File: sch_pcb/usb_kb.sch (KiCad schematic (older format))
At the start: 6 parts, among them P1 USB_C_Plug, U1 STM32F103C6Tx, U2 USBLC6-2SC6

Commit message: Андрей изменил схему, добавил стабилизатор
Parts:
- added C1, C3: 1uF, Capacitor_SMD:C_0805_2012Metric_Pad1.15x1.40mm_HandSolder, symbol Device:C
- added C2, C4: 0.1uF, Capacitor_SMD:C_0805_2012Metric_Pad1.15x1.40mm_HandSolder, symbol Device:C
- added D1: D_Schottky, Diode_SMD:D_SMA, symbol Device:D_Schottky
- added U3: AMS1117-3.3, Package_TO_SOT_SMD:SOT-223-3_TabPin2, symbol Regulator_Linear:AMS1117-3.3
- P1: symbol Connector:USB_C_Plug -> usb_kb-rescue:USB_C_Plug-Connector
- U2: value USBLC6-2SC6 -> AMS1117-3.3; footprint Package_TO_SOT_SMD:SOT-23-6 -> (none); symbol Power_Protection:USBLC6-2SC6 -> usb_kb-rescue:USBLC6-2SC6-Power_Protection
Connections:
- net labels added: +3.3V
- wire segments 26 -> 47
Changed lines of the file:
@@
 $EndDescr
 $Comp
-L Connector:USB_C_Plug P1
+L usb_kb-rescue:USB_C_Plug-Connector P1
 U 1 1 6152BA8E
 P 2100 3100
@@
 $EndComp
 $Comp
-L Power_Protection:USBLC6-2SC6 U2
+L usb_kb-rescue:USBLC6-2SC6-Power_Protection U2
 U 1 1 6153205F
 P 4550 2700
 F 0 "U2" H 4550 3381 50  0000 C CNN
-F 1 "USBLC6-2SC6" H 4550 3290 50  0000 C CNN
-F 2 "Package_TO_SOT_SMD:SOT-23-6" H 3800 3100 50  0001 C CNN
+F 1 "AMS1117-3.3" H 4550 3290 50  0000 C CNN
+F 2 "" H 3800 3100 50  0001 C CNN
 F 3 "http://www2.st.com/resource/en/datasheet/CD00050750.pdf" H 4750 3050 50  0001 C CNN
 	1    4550 2700
@@
 L power:+5V #PWR0101
 U 1 1 61544FD7
-P 2700 1800
-F 0 "#PWR0101" H 2700 1650 50  0001 C CNN
-F 1 "+5V" H 2715 1973 50  0000 C CNN
-F 2 "" H 2700 1800 50  0001 C CNN
-F 3 "" H 2700 1800 50  0001 C CNN
-	1    2700 1800
+P 2900 1300
+F 0 "#PWR0101" H 2900 1150 50  0001 C CNN
+F 1 "+5V" H 2915 1473 50  0000 C CNN
+F 2 "" H 2900 1300 50  0001 C CNN
+F 3 "" H 2900 1300 50  0001 C CNN
+	1    2900 1300
 	1    0    0    -1
 $EndComp
@@
 Wire Wire Line
 	5100 2700 5100 2900
-Wire Wire Line
-	2700 1800 2700 2100
 $Comp
 L power:GNDD #PWR0103
@@
 Wire Wire Line
 	9350 4350 9650 4350
+$Comp
+L Device:C C2
+U 1 1 61570A54
+P 4100 4700
+F 0 "C2" H 4215 4746 50  0000 L CNN
+F 1 "0.1uF" H 4215 4655 50  0000 L CNN
+F 2 "Capacitor_SMD:C_0805_2012Metric_Pad1.15x1.40mm_HandSolder" H 4138 4550 50  0001 C CNN
+F 3 "~" H 4100 4700 50  0001 C CNN
+	1    4100 4700
+	1    0    0    -1
+$EndComp
+$Comp
+L power:+5V #PWR0107
+U 1 1 61580B5F
+P 3750 4300
+F 0 "#PWR0107" H 3750 4150 50  0001 C CNN
+F 1 "+5V" H 3765 4473 50  0000 C CNN
+F 2 "" H 3750 4300 50  0001 C CNN
+F 3 "" H 3750 4300 50  0001 C CNN
+	1    3750 4300
+	1    0    0    -1
+$EndComp
+Wire Wire Line
+	4100 4850 4100 4950
+Wire Wire Line
+	4100 4950 3750 4950
+Wire Wire Line
+	3750 4950 3750 4850
+$Comp
+L power:GNDD #PWR01
+U 1 1 6155592B
+P 3750 5100
+F 0 "#PWR01" H 3750 4850 50  0001 C CNN
+F 1 "GNDD" H 3754 4945 50  0000 C CNN
+F 2 "" H 3750 5100 50  0001 C CNN
+F 3 "" H 3750 5100 50  0001 C CNN
+	1    3750 5100
+	1    0    0    -1
+$EndComp
+Wire Wire Line
+	3750 4950 3750 5100
+Connection ~ 3750 4950
+$Comp
+L power:+3.3V #PWR03
+U 1 1 615606CF
+P 5550 4300
+F 0 "#PWR03" H 5550 4150 50  0001 C CNN
+F 1 "+3.3V" H 5565 4473 50  0000 C CNN
+F 2 "" H 5550 4300 50  0001 C CNN
+F 3 "" H 5550 4300 50  0001 C CNN
+	1    5550 4300
+	1    0    0    -1
+$EndComp
+Wire Wire Line
+	4950 4450 5200 4450
+Wire Wire Line
+	4350 4450 4100 4450
+Wire Wire Line
+	3750 4450 3750 4550
+Wire Wire Line
+	3750 4300 3750 4450
+Connection ~ 3750 4450
+Wire Wire Line
+	4100 4550 4100 4450
+Connection ~ 4100 4450
+Wire Wire Line
+	4100 4450 3750 4450
+Wire Wire Line
+	5200 4550 5200 4450
+Connection ~ 5200 4450
+Wire Wire Line
+	5200 4450 5550 4450
+Wire Wire Line
+	5550 4550 5550 4450
+Wire Wire Line
+	5200 4850 5200 4950
+Wire Wire Line
+	5200 4950 5550 4950
+Wire Wire Line
+	5550 4950 5550 4850
+$Comp
+L power:GNDD #PWR02
+U 1 1 615895AD
+P 4650 5100
+F 0 "#PWR02" H 4650 4850 50  0001 C CNN
+F 1 "GNDD" H 4654 4945 50  0000 C CNN
+F 2 "" H 4650 5100 50  0001 C CNN
+F 3 "" H 4650 5100 50  0001 C CNN
+	1    4650 5100
+	1    0    0    -1
+$EndComp
+$Comp
+L power:GNDD #PWR04
+U 1 1 6158D0F6
+P 5550 5100
+F 0 "#PWR04" H 5550 4850 50  0001 C CNN
+F 1 "GNDD" H 5554 4945 50  0000 C CNN
+F 2 "" H 5550 5100 50  0001 C CNN
+F 3 "" H 5550 5100 50  0001 C CNN
+	1    5550 5100
+	1    0    0    -1
+$EndComp
+Wire Wire Line
+	4650 4750 4650 5100
+Wire Wire Line
+	5550 4950 5550 5100
+Connection ~ 5550 4950
+$Comp
+L Device:C C1
+U 1 1 6159B622
+P 3750 4700
+F 0 "C1" H 3865 4746 50  0000 L CNN
+F 1 "1uF" H 3865 4655 50  0000 L CNN
+F 2 "Capacitor_SMD:C_0805_2012Metric_Pad1.15x1.40mm_HandSolder" H 3788 4550 50  0001 C CNN
+F 3 "~" H 3750 4700 50  0001 C CNN
+	1    3750 4700
+	1    0    0    -1
+$EndComp
+$Comp
+L Device:C C4
+U 1 1 615A45E7
+P 5550 4700
+F 0 "C4" H 5665 4746 50  0000 L CNN
+F 1 "0.1uF" H 5665 4655 50  0000 L CNN
+F 2 "Capacitor_SMD:C_0805_2012Metric_Pad1.15x1.40mm_HandSolder" H 5588 4550 50  0001 C CNN
+F 3 "~" H 5550 4700 50  0001 C CNN
+	1    5550 4700
+	1    0    0    -1
+$EndComp
+$Comp
+L Device:C C3
+U 1 1 615A45ED
+P 5200 4700
+F 0 "C3" H 5315 4746 50  0000 L CNN
+F 1 "1uF" H 5315 4655 50  0000 L CNN
+F 2 "Capacitor_SMD:C_0805_2012Metric_Pad1.15x1.40mm_HandSolder" H 5238 4550 50  0001 C CNN
+F 3 "~" H 5200 4700 50  0001 C CNN
+	1    5200 4700
+	1    0    0    -1
+$EndComp
+Wire Wire Line
+	5550 4300 5550 4450
+Connection ~ 5550 4450
+$Comp
+L Regulator_Linear:AMS1117-3.3 U3
+U 1 1 615B256A
+P 4650 4450
+F 0 "U3" H 4650 4692 50  0000 C CNN
+F 1 "AMS1117-3.3" H 4650 4601 50  0000 C CNN
+F 2 "Package_TO_SOT_SMD:SOT-223-3_TabPin2" H 4650 4650 50  0001 C CNN
+F 3 "http://www.advanced-monolithic.com/pdf/ds1117.pdf" H 4750 4200 50  0001 C CNN
+	1    4650 4450
+	1    0    0    -1
+$EndComp
+$Comp
+L Device:D_Schottky D1
+U 1 1 615BE243
+P 2900 1650
+F 0 "D1" V 2854 1729 50  0000 L CNN
+F 1 "D_Schottky" V 2945 1729 50  0000 L CNN
+F 2 "Diode_SMD:D_SMA" H 2900 1650 50  0001 C CNN
+F 3 "~" H 2900 1650 50  0001 C CNN
+	1    2900 1650
+	0    1    1    0
+$EndComp
+Wire Wire Line
+	2700 2100 2900 2100
+Wire Wire Line
+	2900 2100 2900 1800
+Wire Wire Line
+	2900 1500 2900 1300
 $EndSCHEMATC

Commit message: Андрей добавил питание, Никита доделал
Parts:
- added C10, C9: 20pF, Capacitor_SMD:C_0805_2012Metric_Pad1.15x1.40mm_HandSolder, symbol Device:C
- added C11, C5, C6, C7, C8: 100nF, Capacitor_SMD:C_0805_2012Metric_Pad1.15x1.40mm_HandSolder, symbol Device:C
- added C12, C13: 47nF, Capacitor_SMD:C_0805_2012Metric_Pad1.15x1.40mm_HandSolder, symbol Device:C
- added JP2: Jumper, Jumper:SolderJumper-2_P1.3mm_Open_TrianglePad1.0x1.5mm, symbol Device:Jumper
- added R3, R6: 10k, Resistor_SMD:R_0603_1608Metric_Pad1.05x0.95mm_HandSolder, symbol Device:R
- added R4: 1M, Resistor_SMD:R_0603_1608Metric_Pad1.05x0.95mm_HandSolder, symbol Device:R
- added R5: 1.5k, Resistor_SMD:R_0603_1608Metric_Pad1.05x0.95mm_HandSolder, symbol Device:R
- added X1: 8MHz, Crystal:Crystal_HC49-4H_Vertical, symbol Device:Crystal
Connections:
- net +3V3: now also U1.24 (VDD), U1.36 (VDD), U1.48 (VDD), U1.9 (VDDA), U2.5 (VBUS), C5.1, C6.1, C7.1, C8.1, JP2.2, R3.1, R5.1
- net GNDD: now also U1.23 (VSS), U1.35 (VSS), U1.47 (VSS), U1.8 (VSSA), C10.2, C11.2, C12.2, C13.2, C5.2, C6.2, C7.2, C8.2, C9.2, R6.2
- net USB_D+: now also U2.1 (IO1), U2.6 (IO1), C13.1, R5.2
- net USB_D-: now also U2.3 (IO2), U2.4 (IO2), C12.1
- net at P1.A6 (D+), R2.2: no longer U2.1 (IO1), U2.6 (IO1)
- net at P1.A7 (D-), R1.2: no longer U2.3 (IO2), U2.4 (IO2)
- net at U1.1 (VBAT): now also JP2.1
- net BOOT0: now reaches U1.44 (BOOT0)
- net BOOT0: now also R6.1
- net at U1.5 (PD0): now also C9.1, R4.1, X1.1
- net at U1.6 (PD1): now also C10.1, R4.2, X1.2
- net RST: now reaches U1.7 (NRST)
- net RST: now also C11.1, R3.2
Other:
- moved on the sheet: C1, C2, C3, C4, R1, R2, U1, U3

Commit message: Добавлена кнопа и мелкие правки
Добавлена кнопа и мелкие правки

Co-Authored-By: Andrey2312 <91528901+Andrey2312@users.noreply.github.com>
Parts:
- removed U2: AMS1117-3.3, symbol usb_kb-rescue:USBLC6-2SC6-Power_Protection
- added C14: 0.1uF, Capacitor_SMD:C_0805_2012Metric_Pad1.15x1.40mm_HandSolder, symbol Device:C
- added D2, D3, D4: LED_ALT, Diode_SMD:D_0805_2012Metric_Pad1.15x1.40mm_HandSolder, symbol Device:LED_ALT
- added J1: Conn_01x04_Female, Connector_PinHeader_2.54mm:PinHeader_1x04_P2.54mm_Vertical, symbol Connector:Conn_01x04_Female
- added R10: 10k, Resistor_SMD:R_0603_1608Metric_Pad1.05x0.95mm_HandSolder, symbol Device:R
- added R11, R7, R8: 510, Resistor_SMD:R_0603_1608Metric_Pad1.05x0.95mm_HandSolder, symbol Device:R
- added R9: 100, Resistor_SMD:R_0603_1608Metric_Pad1.05x0.95mm_HandSolder, symbol Device:R
- added SW1: SW_Push, Button_Switch_Keyboard:SW_Cherry_MX_1.00u_PCB, symbol Switch:SW_Push
- added U2: USBLC6-2SC6, Package_TO_SOT_SMD:SOT-23-6, symbol Power_Protection:USBLC6-2SC6
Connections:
- net labels added: Button1, Button2
- wire segments 114 -> 140
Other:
- note added: "НЕ МЕНЯЙ ЭЛЕМЕНТЫ НА 0603 В КОТОРЫХ НЕ УВЕРЕН!!!"
- note added: "Разъём программирования"
- note added: "Сюда повторить кнопку, которая сверху"
- moved on the sheet: C1, C2, C3, C4, R6, U3

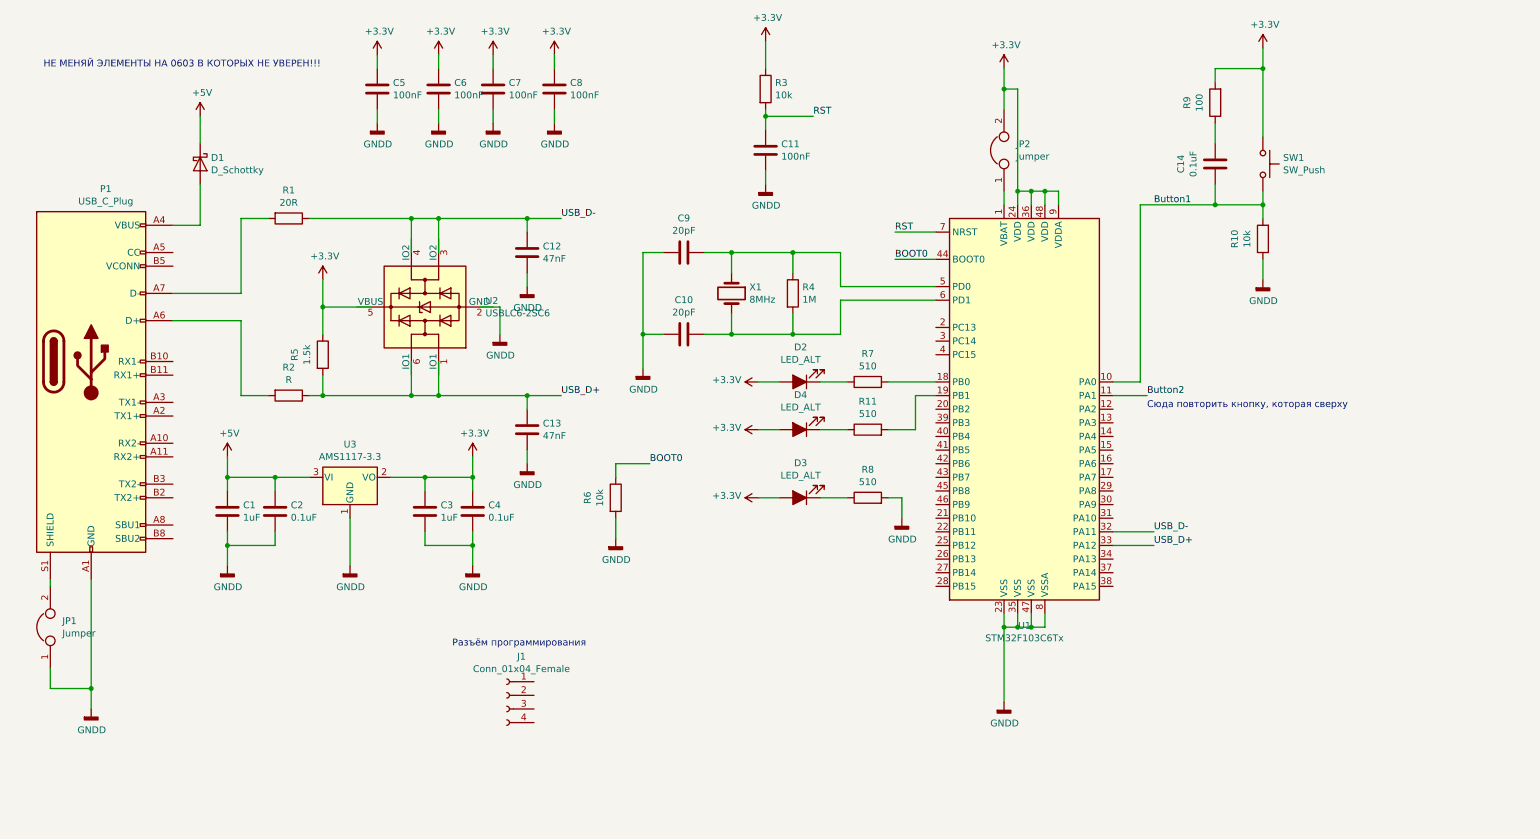
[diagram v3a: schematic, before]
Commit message: ошибка R11. Конечный вариант
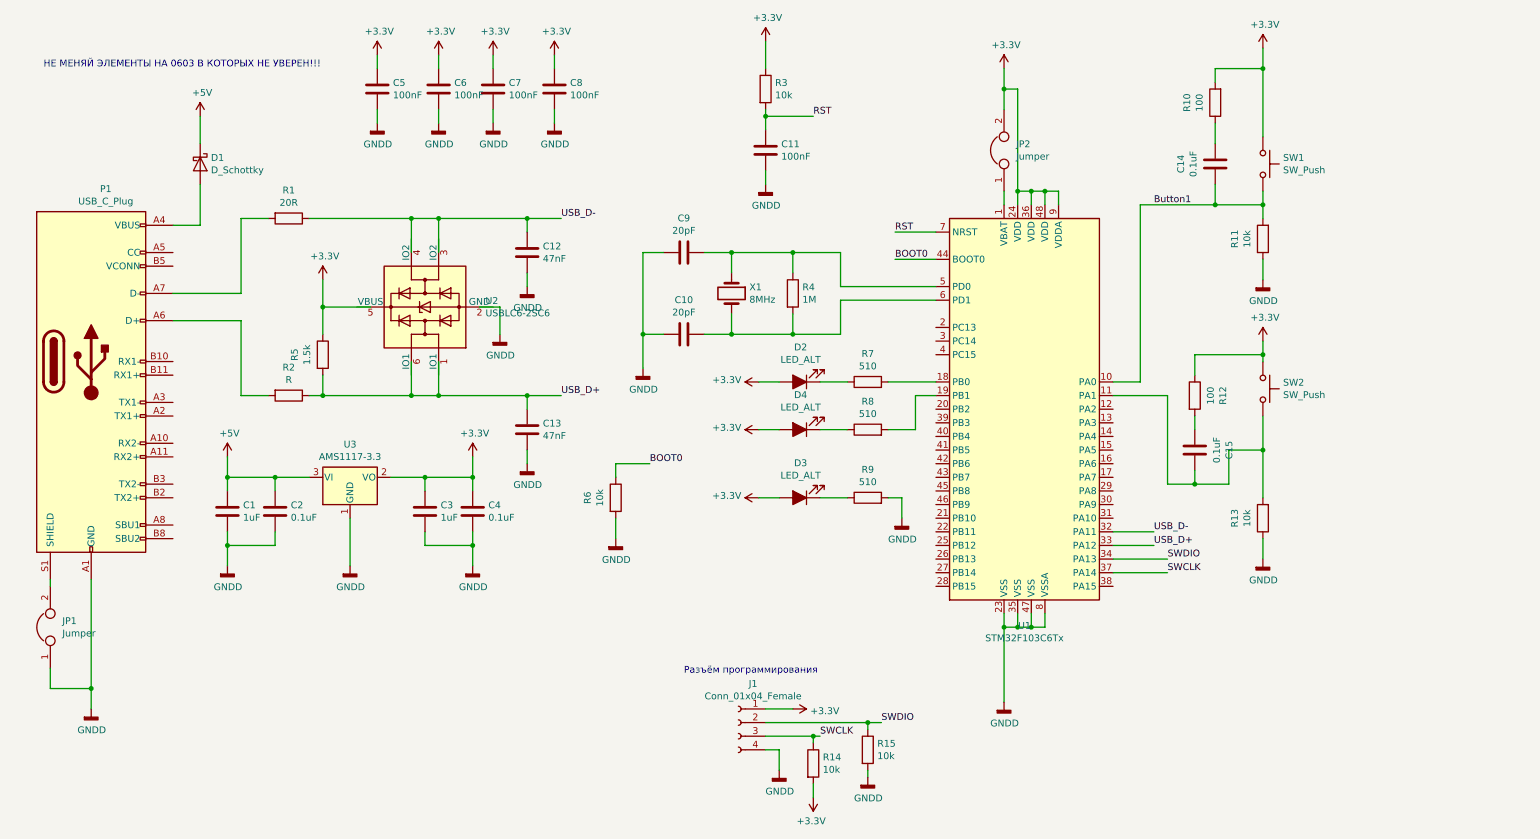
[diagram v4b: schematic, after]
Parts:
- added C15: 0.1uF, Capacitor_SMD:C_0805_2012Metric_Pad1.15x1.40mm_HandSolder, symbol Device:C
- added R12: 100, Resistor_SMD:R_0603_1608Metric_Pad1.05x0.95mm_HandSolder, symbol Device:R
- added R13, R14, R15: 10k, Resistor_SMD:R_0603_1608Metric_Pad1.05x0.95mm_HandSolder, symbol Device:R
- added SW2: SW_Push, Button_Switch_Keyboard:SW_Cherry_MX_1.00u_PCB, symbol Switch:SW_Push
- renumbered R9 to R10, R10 to R11, R11 to R8, R8 to R9
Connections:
- net labels added: SWCLK, SWDIO
- net labels removed: Button2
- wire segments 140 -> 167
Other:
- note removed: "Сюда повторить кнопку, которая сверху"
- moved on the sheet: J1
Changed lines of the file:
@@
 $EndComp
 $Comp
-L Device:R R8
+L Device:R R9
 U 1 1 615BC881
 P 7800 4100
-F 0 "R8" V 8007 4100 50  0000 C CNN
+F 0 "R9" V 8007 4100 50  0000 C CNN
 F 1 "510" V 7916 4100 50  0000 C CNN
 F 2 "Resistor_SMD:R_0603_1608Metric_Pad1.05x0.95mm_HandSolder" V 7730 4100 50  0001 C CNN
@@
 $EndComp
 $Comp
-L Device:R R9
+L Device:R R10
 U 1 1 61563424
 P 10350 1200
-F 0 "R9" V 10557 1200 50  0000 C CNN
+F 0 "R10" V 10557 1200 50  0000 C CNN
 F 1 "100" V 10466 1200 50  0000 C CNN
 F 2 "Resistor_SMD:R_0603_1608Metric_Pad1.05x0.95mm_HandSolder" V 10280 1200 50  0001 C CNN
@@
 $EndComp
 $Comp
-L Device:R R10
+L Device:R R11
 U 1 1 61567374
 P 10700 2200
-F 0 "R10" V 10907 2200 50  0000 C CNN
+F 0 "R11" V 10907 2200 50  0000 C CNN
 F 1 "10k" V 10816 2200 50  0000 C CNN
 F 2 "Resistor_SMD:R_0603_1608Metric_Pad1.05x0.95mm_HandSolder" V 10630 2200 50  0001 C CNN
@@
 Text Label 9900 1950 0    50   ~ 0
 Button1
-Text Label 9850 3350 0    50   ~ 0
-Button2
-Wire Wire Line
-	9850 3350 9600 3350
 $Comp
 L Device:LED_ALT D4
@@
 $EndComp
 $Comp
-L Device:R R11
+L Device:R R8
 U 1 1 615B3C09
 P 7800 3600
-F 0 "R11" V 8007 3600 50  0000 C CNN
+F 0 "R8" V 8007 3600 50  0000 C CNN
 F 1 "510" V 7916 3600 50  0000 C CNN
 F 2 "Resistor_SMD:R_0603_1608Metric_Pad1.05x0.95mm_HandSolder" V 7730 3600 50  0001 C CNN
@@
 Wire Wire Line
 	7950 3250 8300 3250
-Text Notes 9850 3450 0    50   ~ 0
-Сюда повторить кнопку, которая сверху
-$Comp
-L Connector:Conn_01x04_Female J1
-U 1 1 615DD6C5
-P 5150 5550
-F 0 "J1" H 5042 5835 50  0000 C CNN
-F 1 "Conn_01x04_Female" H 5042 5744 50  0000 C CNN
-F 2 "Connector_PinHeader_2.54mm:PinHeader_1x04_P2.54mm_Vertical" H 5150 5550 50  0001 C CNN
-F 3 "~" H 5150 5550 50  0001 C CNN
-	1    5150 5550
-	-1   0    0    -1
-$EndComp
-Text Notes 4750 5200 0    50   ~ 0
-Разъём программирования
 Text Notes 1750 950  0    50   ~ 0
 НЕ МЕНЯЙ ЭЛЕМЕНТЫ НА 0603 В КОТОРЫХ НЕ УВЕРЕН!!!
@@
 Wire Wire Line
 	3800 2700 4150 2700
+$Comp
+L Switch:SW_Push SW2
+U 1 1 615AD94E
+P 10700 3300
+F 0 "SW2" V 10654 3448 50  0000 L CNN
+F 1 "SW_Push" V 10745 3448 50  0000 L CNN
+F 2 "Button_Switch_Keyboard:SW_Cherry_MX_1.00u_PCB" H 10700 3500 50  0001 C CNN
+F 3 "~" H 10700 3500 50  0001 C CNN
+	1    10700 3300
+	0    1    1    0
+$EndComp
+$Comp
+L Device:R R13
+U 1 1 615C8D27
+P 10700 4250
+F 0 "R13" V 10907 4250 50  0000 C CNN
+F 1 "10k" V 10816 4250 50  0000 C CNN
+F 2 "Resistor_SMD:R_0603_1608Metric_Pad1.05x0.95mm_HandSolder" V 10630 4250 50  0001 C CNN
+F 3 "~" H 10700 4250 50  0001 C CNN
+	1    10700 4250
+	-1   0    0    1
+$EndComp
+$Comp
+L power:GNDD #PWR031
+U 1 1 615C8D2D
+P 10700 4550
+F 0 "#PWR031" H 10700 4300 50  0001 C CNN
+F 1 "GNDD" H 10704 4395 50  0000 C CNN
+F 2 "" H 10700 4550 50  0001 C CNN
+F 3 "" H 10700 4550 50  0001 C CNN
+	1    10700 4550
+	1    0    0    -1
+$EndComp
+Wire Wire Line
+	10700 4550 10700 4400
+$Comp
+L power:+3.3V #PWR030
+U 1 1 61704C01
+P 10700 2950
+F 0 "#PWR030" H 10700 2800 50  0001 C CNN
+F 1 "+3.3V" H 10715 3123 50  0000 C CNN
+F 2 "" H 10700 2950 50  0001 C CNN
+F 3 "" H 10700 2950 50  0001 C CNN
+	1    10700 2950
+	1    0    0    -1
+$EndComp
+Wire Wire Line
+	10700 3100 10700 3050
+$Comp
+L Device:R R12
+U 1 1 61584F00
+P 10200 3350
+F 0 "R12" V 10407 3350 50  0000 C CNN
+F 1 "100" V 10316 3350 50  0000 C CNN
+F 2 "Resistor_SMD:R_0603_1608Metric_Pad1.05x0.95mm_HandSolder" V 10130 3350 50  0001 C CNN
+F 3 "~" H 10200 3350 50  0001 C CNN
+	1    10200 3350
+	1    0    0    -1
+$EndComp
+$Comp
+L Device:C C15
+U 1 1 61594438
+P 10200 3750
+F 0 "C15" V 9948 3750 50  0000 C CNN
+F 1 "0.1uF" V 10039 3750 50  0000 C CNN
+F 2 "Capacitor_SMD:C_0805_2012Metric_Pad1.15x1.40mm_HandSolder" H 10238 3600 50  0001 C CNN
+F 3 "~" H 10200 3750 50  0001 C CNN
+	1    10200 3750
+	-1   0    0    1
+$EndComp
+Wire Wire Line
+	10000 3350 9600 3350
+Wire Wire Line
+	10200 3200 10200 3050
+Wire Wire Line
+	10200 3050 10700 3050
+Connection ~ 10700 3050
+Wire Wire Line
+	10700 3050 10700 2950
+Wire Wire Line
+	10700 3500 10700 3750
+Wire Wire Line
+	10450 4000 10450 3750
+Wire Wire Line
+	10450 3750 10700 3750
+Wire Wire Line
+	10000 4000 10200 4000
+Wire Wire Line
+	10000 4000 10000 3350
+Connection ~ 10700 3750
+Wire Wire Line
+	10700 3750 10700 4100
+Wire Wire Line
+	10200 3900 10200 4000
+Connection ~ 10200 4000
+Wire Wire Line
+	10200 4000 10450 4000
+Wire Wire Line
+	10200 3500 10200 3600
+Wire Wire Line
+	7050 5950 7150 5950
+Wire Wire Line
+	7150 5950 7150 6100
+$Comp
+L power:GNDD #PWR028
+U 1 1 615C7D1A
+P 7150 6100
+F 0 "#PWR028" H 7150 5850 50  0001 C CNN
+F 1 "GNDD" H 7154 5945 50  0000 C CNN
+F 2 "" H 7150 6100 50  0001 C CNN
+F 3 "" H 7150 6100 50  0001 C CNN
+	1    7150 6100
+	1    0    0    -1
+$EndComp
+Wire Wire Line
+	7050 5650 7250 5650
+$Comp
+L power:+3.3V #PWR029
+U 1 1 615B9365
+P 7250 5650
+F 0 "#PWR029" H 7250 5500 50  0001 C CNN
+F 1 "+3.3V" V 7265 5778 50  0000 L CNN
+F 2 "" H 7250 5650 50  0001 C CNN
+F 3 "" H 7250 5650 50  0001 C CNN
+	1    7250 5650
+	0    1    1    0
+$EndComp
+Text Notes 6450 5400 0    50   ~ 0
+Разъём программирования
+$Comp
+L Connector:Conn_01x04_Female J1
+U 1 1 615DD6C5
+P 6850 5750
+F 0 "J1" H 6742 6035 50  0000 C CNN
+F 1 "Conn_01x04_Female" H 6742 5944 50  0000 C CNN
+F 2 "Connector_PinHeader_2.54mm:PinHeader_1x04_P2.54mm_Vertical" H 6850 5750 50  0001 C CNN
+F 3 "~" H 6850 5750 50  0001 C CNN
+	1    6850 5750
+	-1   0    0    -1
+$EndComp
+Text Label 7900 5750 0    50   ~ 0
+SWDIO
+Wire Wire Line
+	7050 5750 7800 5750
+Text Label 10000 4550 0    50   ~ 0
+SWDIO
+Wire Wire Line
+	9600 4550 10000 4550
+Text Label 7450 5850 0    50   ~ 0
+SWCLK
+Wire Wire Line
+	7050 5850 7400 5850
+Text Label 10000 4650 0    50   ~ 0
+SWCLK
+Wire Wire Line
+	9600 4650 10000 4650
+$Comp
+L Device:R R15
+U 1 1 616A4701
+P 7800 5950
+F 0 "R15" H 7870 5996 50  0000 L CNN
+F 1 "10k" H 7870 5905 50  0000 L CNN
+F 2 "Resistor_SMD:R_0603_1608Metric_Pad1.05x0.95mm_HandSolder" V 7730 5950 50  0001 C CNN
+F 3 "~" H 7800 5950 50  0001 C CNN
+	1    7800 5950
+	1    0    0    -1
+$EndComp
+$Comp
+L Device:R R14
+U 1 1 616A5D0F
+P 7400 6050
+F 0 "R14" H 7470 6096 50  0000 L CNN
+F 1 "10k" H 7470 6005 50  0000 L CNN
+F 2 "Resistor_SMD:R_0603_1608Metric_Pad1.05x0.95mm_HandSolder" V 7330 6050 50  0001 C CNN
+F 3 "~" H 7400 6050 50  0001 C CNN
+	1    7400 6050
+	1    0    0    -1
+$EndComp
+$Comp
+L power:GNDD #PWR0104
+U 1 1 616B3CB3
+P 7800 6150
+F 0 "#PWR0104" H 7800 5900 50  0001 C CNN
+F 1 "GNDD" H 7804 5995 50  0000 C CNN
+F 2 "" H 7800 6150 50  0001 C CNN
+F 3 "" H 7800 6150 50  0001 C CNN
+	1    7800 6150
+	1    0    0    -1
+$EndComp
+Wire Wire Line
+	7800 6100 7800 6150
+Wire Wire Line
+	7800 5800 7800 5750
+Connection ~ 7800 5750
+Wire Wire Line
+	7800 5750 7900 5750
+Wire Wire Line
+	7400 5850 7400 5900
+Connection ~ 7400 5850
+Wire Wire Line
+	7400 5850 7450 5850
+$Comp
+L power:+3.3V #PWR0105
+U 1 1 616C9CD5
+P 7400 6300
+F 0 "#PWR0105" H 7400 6150 50  0001 C CNN
+F 1 "+3.3V" H 7415 6473 50  0000 C CNN
+F 2 "" H 7400 6300 50  0001 C CNN
+F 3 "" H 7400 6300 50  0001 C CNN
+	1    7400 6300
+	-1   0    0    1
+$EndComp
+Wire Wire Line
+	7400 6200 7400 6300
 $EndSCHEMATC
